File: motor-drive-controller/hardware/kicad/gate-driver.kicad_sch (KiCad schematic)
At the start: 12 parts, among them U3 DRV83053PHP

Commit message: feat(hw09): create links between labels of different hierarchical sheets
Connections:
- net DRV_PWRGD: no longer U3.13 (PWRGD)
- net DRV_nFAULT: no longer U3.8 (~{FAULT})
- net DRV_SCLK renamed DRV.SCLK
- net DRV_SDI renamed DRV.SDI
- net DRV_SDO renamed DRV.SDO
- net DRV_nSCS renamed DRV.nSCS
- net GHA renamed GATE.GHA
- net GHB renamed GATE.GHB
- net GHC renamed GATE.GHC
- net GLA renamed GATE.GLA
- net GLB renamed GATE.GLB
- net GLC renamed GATE.GLC
- net INHA renamed DRV.INHA
- net INHB renamed DRV.INHB
- net INHC renamed DRV.INHC
- net INLA renamed DRV.INLA
- net INLB renamed DRV.INLB
- net INLC renamed DRV.INLC
- net PHASE_A renamed PH.SHA
- net PHASE_B renamed PH.SHB
- net PHASE_C renamed PH.SHC
- net SLA renamed PH.SLA
- net SLB renamed PH.SLB
- net SLC renamed PH.SLC
- net SN_HA renamed CS.SN_LA
- net SN_HB renamed CS.SN_LB
- net SN_HC renamed CS.SN_LC
- net SN_LA renamed CS.SN_HA
- net SN_LB renamed CS.SN_HB
- net SN_LC renamed CS.SN_HC
- new net DRV.PWRGD: U3.13 (PWRGD)
- new net DRV.nFAULT: U3.8 (~{FAULT})
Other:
- moved on the sheet: C16, C17, C20, C21, C24, R12, R15, R16

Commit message: feat(hw09): rename net labels
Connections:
- net DRV_PWRGD is gone; now on net DRV.PWRGD: R16.2
- net DRV_nFAULT is gone; now on net DRV.nFAULT: R15.2
- net CS.SN_HA: now also U3.23 (SN1); no longer U3.24 (SP1)
- net CS.SN_HB: now also U3.21 (SN2); no longer U3.22 (SP2)
- net CS.SN_HC: now also U3.19 (SN3); no longer U3.20 (SP3)
- net CS.SN_LA: now also U3.24 (SP1); no longer U3.23 (SN1)
- net CS.SN_LB: now also U3.22 (SP2); no longer U3.21 (SN2)
- net CS.SN_LC: now also U3.20 (SP3); no longer U3.19 (SN3)
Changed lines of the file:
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@@
+	)
+	(bus_entry
+		(at 95.25 78.74)
+		(size 2.54 2.54)
+		(stroke
+			(width 0)
+			(type default)
+		)
 	)
 	(bus_entry
@@
 	)
 	(bus_entry
+		(at 95.25 96.52)
+		(size 2.54 2.54)
+		(stroke
+			(width 0)
+			(type default)
+		)
+	)
+	(bus_entry
 		(at 95.25 132.08)
 		(size 2.54 2.54)
@@
 	)
 	(bus_entry
+		(at 95.25 81.28)
+		(size 2.54 2.54)
+		(stroke
+			(width 0)
+			(type default)
+		)
+	)
+	(bus_entry
 		(at 158.75 68.58)
 		(size -2.54 -2.54)
@@
 	)
 	(bus_entry
-		(at 95.25 78.74)
-		(size 2.54 2.54)
-		(stroke
-			(width 0)
-			(type default)
-		)
-	)
-	(bus_entry
-		(at 95.25 88.9)
+		(at 95.25 93.98)
 		(size 2.54 2.54)
 		(stroke
@@
 	(bus_entry
 		(at 95.25 66.04)
-		(size 2.54 2.54)
-		(stroke
-			(width 0)
-			(type default)
-		)
-	)
-	(bus_entry
-		(at 95.25 81.28)
 		(size 2.54 2.54)
 		(stroke
@@
 	)
 	(bus_entry
+		(at 95.25 88.9)
+		(size 2.54 2.54)
+		(stroke
+			(width 0)
+			(type default)
+		)
+	)
+	(bus_entry
+		(at 95.25 86.36)
+		(size 2.54 2.54)
+		(stroke
+			(width 0)
+			(type default)
+		)
+	)
+	(bus_entry
 		(at 158.75 63.5)
 		(size -2.54 -2.54)
@@
 	)
 	(bus_entry
-		(at 95.25 93.98)
-		(size 2.54 2.54)
-		(stroke
-			(width 0)
-			(type default)
-		)
-	)
-	(bus_entry
-		(at 95.25 86.36)
-		(size 2.54 2.54)
-		(stroke
-			(width 0)
-			(type default)
-		)
-	)
-	(bus_entry
 		(at 95.25 119.38)
 		(size 2.54 2.54)
@@
 	)
 	(bus_entry
-		(at 95.25 96.52)
-		(size 2.54 2.54)
-		(stroke
-			(width 0)
-			(type default)
-		)
-	)
-	(bus_entry
 		(at 95.25 129.54)
 		(size 2.54 2.54)
@@
 			(width 0)
 			(type default)
+		)
+	)
+	(label "CS.SN_LB"
+		(at 97.79 91.44 0)
+		(effects
+			(font
+				(size 1.27 1.27)
+			)
+			(justify left bottom)
 		)
 	)
@@
 		)
 	)
+	(label "CS.SN_HC"
+		(at 97.79 96.52 0)
+		(effects
+			(font
+				(size 1.27 1.27)
+			)
+			(justify left bottom)
+		)
+	)
 	(label "GATE.GLB"
 		(at 156.21 68.58 180)
@@
 		)
 	)
-	(label "CS.SN_HA"
-		(at 97.79 83.82 0)
-		(effects
-			(font
-				(size 1.27 1.27)
-			)
-			(justify left bottom)
-		)
-	)
-	(label "CS.SN_LA"
-		(at 97.79 81.28 0)
-		(effects
-			(font
-				(size 1.27 1.27)
-			)
-			(justify left bottom)
-		)
-	)
 	(label "PVDD"
 		(at 265.43 40.64 0)
@@
 	)
 	(label "CS.SN_HB"
-		(at 97.79 91.44 0)
+		(at 97.79 88.9 0)
+		(effects
+			(font
+				(size 1.27 1.27)
+			)
+			(justify left bottom)
+		)
+	)
+	(label "CS.SN_LA"
+		(at 97.79 83.82 0)
 		(effects
 			(font
@@
 		)
 	)
-	(label "DRV_nFAULT"
+	(label "DRV.nFAULT"
 		(at 248.92 143.51 180)
 		(effects
@@
 		)
 	)
+	(label "CS.SN_LC"
+		(at 97.79 99.06 0)
+		(effects
+			(font
+				(size 1.27 1.27)
+			)
+			(justify left bottom)
+		)
+	)
 	(label "DRV.SCLK"
 		(at 97.79 129.54 0)
@@
 		)
 	)
-	(label "CS.SN_LB"
-		(at 97.79 88.9 0)
-		(effects
-			(font
-				(size 1.27 1.27)
-			)
-			(justify left bottom)
-		)
-	)
-	(label "CS.SN_HC"
-		(at 97.79 99.06 0)
-		(effects
-			(font
-				(size 1.27 1.27)
-			)
-			(justify left bottom)
-		)
-	)
-	(label "DRV_PWRGD"
+	(label "DRV.PWRGD"
 		(at 256.54 143.51 0)
 		(effects
@@
 		)
 	)
-	(label "CS.SN_LC"
-		(at 97.79 96.52 0)
-		(effects
-			(font
-				(size 1.27 1.27)
-			)
-			(justify left bottom)
-		)
-	)
 	(label "DRV.INHB"
 		(at 97.79 111.76 0)
 		(effects
 			(font
+				(size 1.27 1.27)
+			)
+			(justify left bottom)
+		)
+	)
+	(label "CS.SN_HA"
+		(at 97.79 81.28 0)
+		(effects
+			(font

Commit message: feat(hw09): add ISENSE ADC channels and update schematics
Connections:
- net ISENSE.SO1: now reaches U3.16 (SO1)
- net ISENSE.SO2: now reaches U3.17 (SO2)
- net ISENSE.SO3: now reaches U3.18 (SO3)
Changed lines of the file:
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@@
+	)
+	(bus_entry
+		(at 158.75 88.9)
+		(size -2.54 -2.54)
+		(stroke
+			(width 0)
+			(type default)
+		)
 	)
 	(bus_entry
@@
 		(at 95.25 96.52)
 		(size 2.54 2.54)
+		(stroke
+			(width 0)
+			(type default)
+		)
+	)
+	(bus_entry
+		(at 158.75 86.36)
+		(size -2.54 -2.54)
 		(stroke
 			(width 0)
@@
 	)
 	(bus_entry
+		(at 158.75 83.82)
+		(size -2.54 -2.54)
+		(stroke
+			(width 0)
+			(type default)
+		)
+	)
+	(bus_entry
 		(at 95.25 129.54)
 		(size 2.54 2.54)
@@
 	(wire
 		(pts
+			(xy 143.51 86.36) (xy 156.21 86.36)
+		)
+		(stroke
+			(width 0)
+			(type default)
+		)
+	)
+	(wire
+		(pts
 			(xy 96.52 147.32) (xy 92.71 147.32)
 		)
@@
 	(wire
 		(pts
+			(xy 143.51 81.28) (xy 156.21 81.28)
+		)
+		(stroke
+			(width 0)
+			(type default)
+		)
+	)
+	(wire
+		(pts
 			(xy 248.92 143.51) (xy 248.92 138.43)
 		)
@@
 	(bus
 		(pts
+			(xy 165.1 91.44) (xy 158.75 91.44)
+		)
+		(stroke
+			(width 0)
+			(type default)
+		)
+	)
+	(bus
+		(pts
 			(xy 95.25 73.66) (xy 95.25 53.34)
 		)
@@
 		)
 	)
+	(wire
+		(pts
+			(xy 143.51 83.82) (xy 156.21 83.82)
+		)
+		(stroke
+			(width 0)
+			(type default)
+		)
+	)
 	(bus
 		(pts
@@
 		(pts
 			(xy 97.79 129.54) (xy 107.95 129.54)
+		)
+		(stroke
+			(width 0)
+			(type default)
+		)
+	)
+	(bus
+		(pts
+			(xy 158.75 83.82) (xy 158.75 91.44)
 		)
 		(stroke
@@
 		)
 	)
+	(label "ISENSE.SO2"
+		(at 156.21 83.82 180)
+		(effects
+			(font
+				(size 1.27 1.27)
+			)
+			(justify right bottom)
+		)
+	)
 	(label "DRV.PWRGD"
 		(at 256.54 143.51 0)
@@
 		)
 	)
+	(label "ISENSE.SO3"
+		(at 156.21 86.36 180)
+		(effects
+			(font
+				(size 1.27 1.27)
+			)
+			(justify right bottom)
+		)
+	)
 	(label "AVDD"
 		(at 247.65 86.36 0)
@@
 			)
 			(justify bottom)
+		)
+	)
+	(label "ISENSE.SO1"
+		(at 156.21 81.28 180)
+		(effects
+			(font
+				(size 1.27 1.27)
+			)
+			(justify right bottom)
 		)
 	)
@@
 		(effects
 			(font
+				(size 1.27 1.27)
+			)
+			(justify left)
+		)
+	)
+	(hierarchical_label "ISENSE{ADC3}"
+		(shape output)
+		(at 165.1 91.44 0)
+		(effects
+			(font

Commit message: feat(hw09): update ADC channel names and schematic references to ANALOG prefix
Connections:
- net ISENSE.SO1 renamed ANALOG.SO1
- net ISENSE.SO2 renamed ANALOG.SO2
- net ISENSE.SO3 renamed ANALOG.SO3
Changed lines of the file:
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@@
 		)
 	)
-	(label "ISENSE.SO2"
+	(label "ANALOG.SO2"
 		(at 156.21 83.82 180)
 		(effects
@@
 		)
 	)
-	(label "ISENSE.SO3"
+	(label "ANALOG.SO3"
 		(at 156.21 86.36 180)
 		(effects
@@
 		)
 	)
-	(label "ISENSE.SO1"
+	(label "ANALOG.SO1"
 		(at 156.21 81.28 180)
 		(effects
@@
 		)
 	)
-	(hierarchical_label "ISENSE{ADC3}"
+	(hierarchical_label "ANALOG{AIN4}"
 		(shape output)
 		(at 165.1 91.44 0)

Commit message: fix(hw09): fix ERC issues
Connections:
- net DRV.EN_GATE: now reaches U3.1 (EN_GATE)
- net DRV.WAKE: now reaches U3.47 (WAKE)
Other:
- moved on the sheet: C16, C17, C18, C19, C20, C23, C24, R12, R15, R16

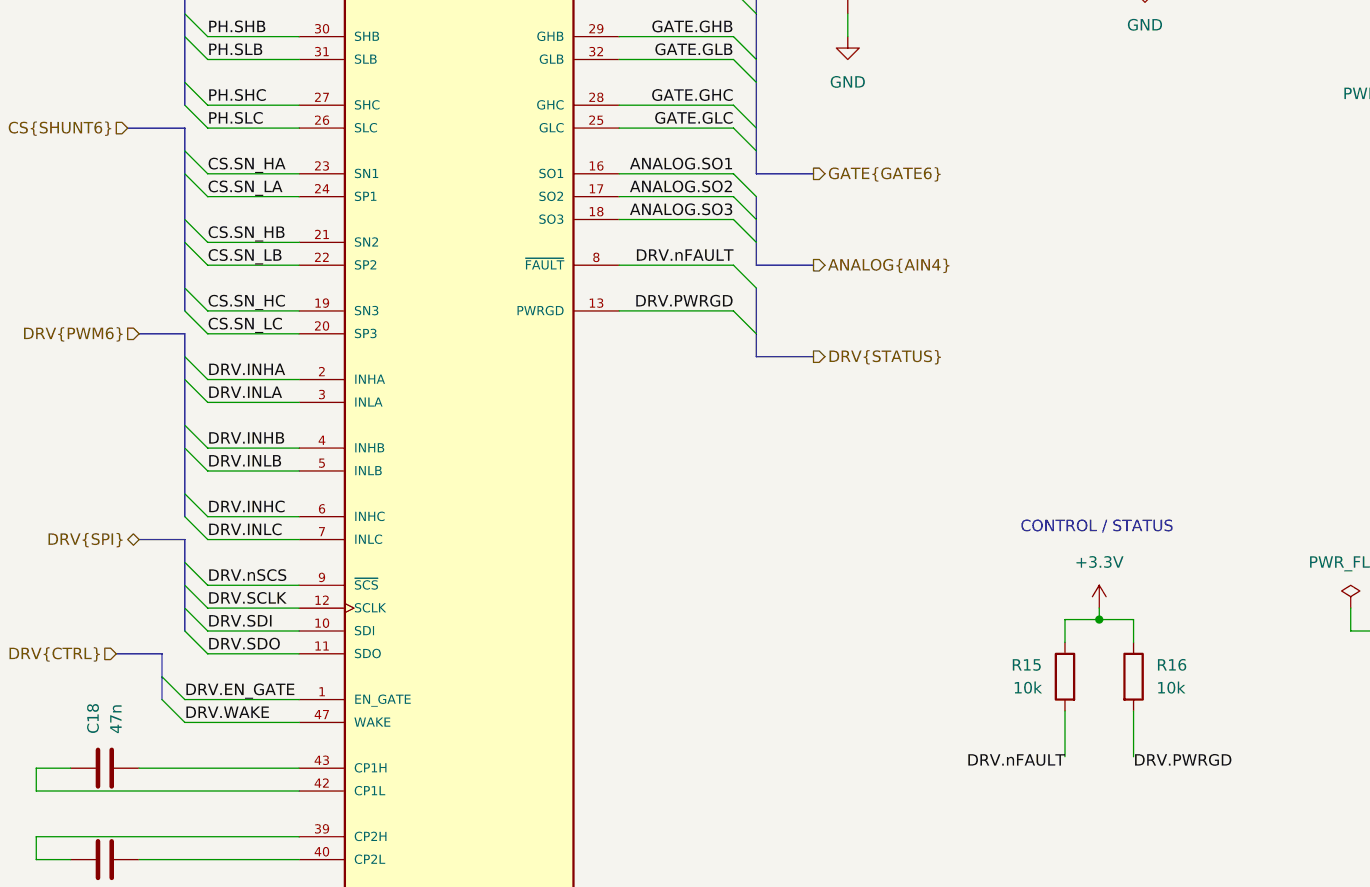
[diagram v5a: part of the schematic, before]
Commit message: feat(hw09): add EN_GATE control and WAKE signal handling in hardware design
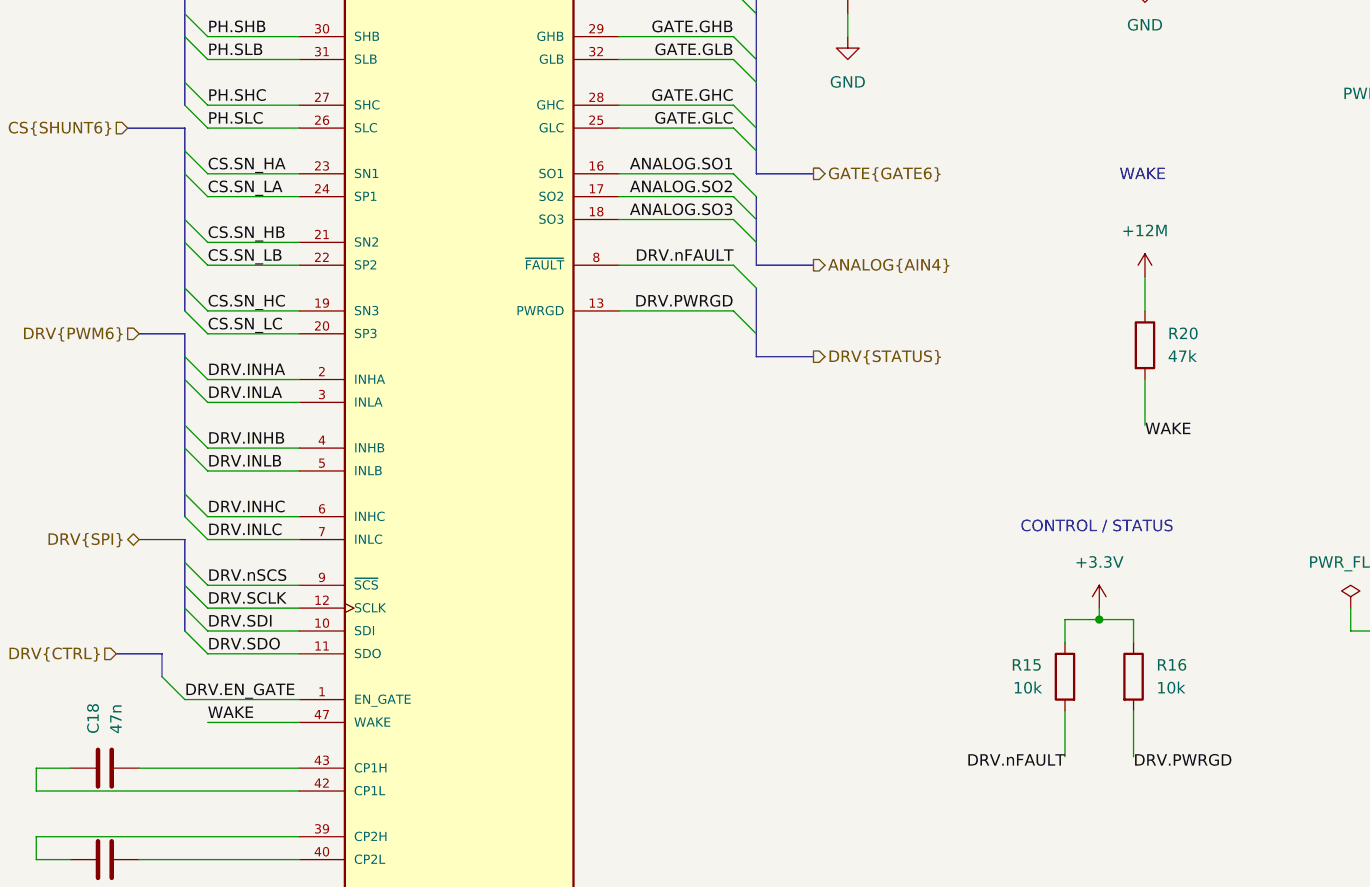
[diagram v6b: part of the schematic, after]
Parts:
- added R20: 47k, symbol Device:R
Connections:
- net +12M: now also R20.1
- net DRV.WAKE renamed WAKE
- net WAKE: now also R20.2
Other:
- note added: "WAKE"
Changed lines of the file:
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@@
 		(title "Gate Driver — DRV8305")
 	)
+	(text "WAKE"
+		(exclude_from_sim no)
+		(at 201.676 81.534 0)
+		(effects
+			(font
+				(size 1.27 1.27)
+			)
+		)
+	)
 	(text "Живлення"
 		(exclude_from_sim no)
@@
 	)
 	(bus_entry
+		(at 92.71 137.16)
+		(size 2.54 2.54)
+		(stroke
+			(width 0)
+			(type default)
+		)
+	)
+	(bus_entry
 		(at 95.25 93.98)
 		(size 2.54 2.54)
@@
 	)
 	(bus_entry
-		(at 92.71 139.7)
-		(size 2.54 2.54)
-		(stroke
-			(width 0)
-			(type default)
-		)
-	)
-	(bus_entry
-		(at 92.71 137.16)
-		(size 2.54 2.54)
-		(stroke
-			(width 0)
-			(type default)
-		)
-	)
-	(bus_entry
 		(at 95.25 129.54)
 		(size 2.54 2.54)
@@
 	(wire
 		(pts
-			(xy 143.51 86.36) (xy 156.21 86.36)
+			(xy 201.93 104.14) (xy 201.93 109.22)
 		)
 		(stroke
@@
 	(wire
 		(pts
-			(xy 224.79 132.08) (xy 237.49 132.08)
+			(xy 143.51 86.36) (xy 156.21 86.36)
 		)
 		(stroke
@@
 	(wire
 		(pts
-			(xy 240.03 62.23) (xy 240.03 68.58)
+			(xy 224.79 132.08) (xy 237.49 132.08)
 		)
 		(stroke
@@
 	(wire
 		(pts
-			(xy 82.55 147.32) (xy 78.74 147.32)
+			(xy 240.03 62.23) (xy 240.03 68.58)
 		)
 		(stroke
@@
 	(wire
 		(pts
-			(xy 95.25 142.24) (xy 107.95 142.24)
+			(xy 82.55 147.32) (xy 78.74 147.32)
 		)
 		(stroke
@@
 		)
 	)
+	(wire
+		(pts
+			(xy 95.25 139.7) (xy 107.95 139.7)
+		)
+		(stroke
+			(width 0)
+			(type default)
+		)
+	)
 	(bus
 		(pts
@@
 	(bus
 		(pts
-			(xy 92.71 139.7) (xy 92.71 134.62)
+			(xy 92.71 137.16) (xy 92.71 134.62)
 		)
 		(stroke
@@
 	(wire
 		(pts
-			(xy 240.03 41.91) (xy 240.03 48.26)
+			(xy 201.93 92.71) (xy 201.93 96.52)
 		)
 		(stroke
@@
 		)
 	)
-	(bus
+	(wire
 		(pts
-			(xy 87.63 134.62) (xy 92.71 134.62)
+			(xy 240.03 41.91) (xy 240.03 48.26)
 		)
 		(stroke
@@
 	(bus
 		(pts
-			(xy 90.17 121.92) (xy 95.25 121.92)
+			(xy 87.63 134.62) (xy 92.71 134.62)
 		)
 		(stroke
@@
 		)
 	)
-	(wire
+	(bus
 		(pts
-			(xy 95.25 139.7) (xy 107.95 139.7)
+			(xy 90.17 121.92) (xy 95.25 121.92)
 		)
 		(stroke
@@
 		)
 	)
+	(wire
+		(pts
+			(xy 97.79 142.24) (xy 107.95 142.24)
+		)
+		(stroke
+			(width 0)
+			(type default)
+		)
+	)
 	(bus
 		(pts
@@
 		)
 	)
-	(label "DRV.EN_GATE"
-		(at 95.25 139.7 0)
+	(label "PVDD"
+		(at 156.21 45.72 180)
 		(effects
 			(font
 				(size 1.27 1.27)
 			)
-			(justify left bottom)
+			(justify right bottom)
 		)
 	)
-	(label "PVDD"
-		(at 156.21 45.72 180)
+	(label "AVDD"
+		(at 156.21 40.64 180)
 		(effects
 			(font
@@
 		)
 	)
-	(label "AVDD"
-		(at 156.21 40.64 180)
+	(label "DRV.EN_GATE"
+		(at 95.25 139.7 0)
 		(effects
 			(font
 				(size 1.27 1.27)
 			)
-			(justify right bottom)
+			(justify left bottom)
 		)
 	)
@@
 		)
 	)
+	(label "WAKE"
+		(at 97.79 142.24 0)
+		(effects
+			(font
+				(size 1.27 1.27)
+			)
+			(justify left bottom)
+		)
+	)
 	(label "PH.SLC"
 		(at 97.79 76.2 0)
@@
 		)
 	)
+	(label "WAKE"
+		(at 201.93 109.22 0)
+		(effects
+			(font
+				(size 1.27 1.27)
+			)
+			(justify top)
+		)
+	)
 	(label "DRV.INLB"
 		(at 97.79 114.3 0)
@@
 		)
 	)
-	(label "DRV.WAKE"
-		(at 95.25 142.24 0)
-		(effects
-			(font
-				(size 1.27 1.27)
-			)
-			(justify left bottom)
-		)
-	)
 	(label "PH.SLB"
 		(at 97.79 68.58 0)
@@
 	)
 	(symbol
+		(lib_id "Device:R")
+		(at 201.93 100.33 0)
+		(unit 1)
+		(body_style 1)
+		(exclude_from_sim no)
+		(in_bom yes)
+		(on_board yes)
+		(in_pos_files yes)
+		(dnp no)
+		(fields_autoplaced yes)
+		(property "Reference" "R20"
+			(at 204.47 99.0599 0)
+			(show_name no)
+			(do_not_autoplace no)
+			(effects
+				(font
+					(size 1.27 1.27)
+				)
+				(justify left)
+			)
+		)
+		(property "Value" "47k"
+			(at 204.47 101.5999 0)
+			(show_name no)
+			(do_not_autoplace no)
+			(effects
+				(font
+					(size 1.27 1.27)
+				)
+				(justify left)
+			)
+		)
+		(property "Footprint" ""
+			(at 200.152 100.33 90)
+			(hide yes)
+			(show_name no)
+			(do_not_autoplace no)
+			(effects
+				(font
+					(size 1.27 1.27)
+				)
+			)
+		)
+		(property "Datasheet" ""
+			(at 201.93 100.33 0)
+			(hide yes)
+			(show_name no)
+			(do_not_autoplace no)
+			(effects
+				(font
+					(size 1.27 1.27)
+				)
+			)
+		)
+		(property "Description" "Resistor"
+			(at 201.93 100.33 0)
+			(hide yes)
+			(show_name no)
+			(do_not_autoplace no)
+			(effects
+				(font
+					(size 1.27 1.27)
+				)
+			)
+		)
+		(pin "1"
+		)
+		(pin "2"
+		)
+		(instances
+			(project "motor-drive-controller"
+				(path "/b8e0307a-d356-4cd3-91c6-dd251b6e910b/0c161995-df7f-44eb-a617-0aa9a9de53ee"
+					(reference "R20")
+					(unit 1)
+				)
+			)
+		)
+	)
+	(symbol
 		(lib_id "power:+3.3V")
 		(at 201.93 43.18 0)
@@
 					(unit 1)
 				)
+			)
+		)
+	)
+	(symbol
+		(lib_id "power:+12V")
+		(at 201.93 92.71 0)
+		(unit 1)
+		(body_style 1)
+		(exclude_from_sim no)
+		(in_bom yes)
+		(on_board yes)
+		(in_pos_files yes)
+		(dnp no)
+		(fields_autoplaced yes)
+		(property "Reference" "#PWR052"
+			(at 201.93 96.52 0)
+			(hide yes)
+			(show_name no)
+			(do_not_autoplace no)
+			(effects
+				(font
+					(size 1.27 1.27)
+				)
+			)
+		)
+		(property "Value" "+12M"
+			(at 201.93 87.63 0)
+			(show_name no)
+			(do_not_autoplace no)
+			(effects
+				(font
+					(size 1.27 1.27)
+				)
+			)
+		)
+		(property "Footprint" ""
+			(at 201.93 92.71 0)
+			(hide yes)
+			(show_name no)
+			(do_not_autoplace no)
+			(effects
+				(font
+					(size 1.27 1.27)
+				)
+			)
+		)
+		(property "Datasheet" ""
+			(at 201.93 92.71 0)
+			(hide yes)
+			(show_name no)
+			(do_not_autoplace no)
+			(effects
+				(font
+					(size 1.27 1.27)
+				)
+			)
+		)
+		(property "Description" "Power symbol creates a global label with name \"+12V\""
+			(at 201.93 92.71 0)
+			(hide yes)
+			(show_name no)
+			(do_not_autoplace no)
+			(effects
+				(font
+					(size 1.27 1.27)
+				)
+			)
+		)
+		(pin "1"
+		)
+		(instances
+			(project "motor-drive-controller"
+				(path "/b8e0307a-d356-4cd3-91c6-dd251b6e910b/0c161995-df7f-44eb-a617-0aa9a9de53ee"
+					(reference "#PWR052")
+					(unit 1)
+				)

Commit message: fix(hw09): fix ERC issues
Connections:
- net GND is gone; now on net EP: C16.2, C17.2, C20.2, C23.2, C24.2, U3.14 (GND), U3.45 (GND)
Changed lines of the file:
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@@
 	)
 	(junction
+		(at 148.59 165.1)
+		(diameter 0)
+		(color 0 0 0 0)
+	)
+	(junction
 		(at 237.49 132.08)
 		(diameter 0)
@@
 	(wire
 		(pts
+			(xy 191.77 43.18) (xy 191.77 45.72)
+		)
+		(stroke
+			(width 0)
+			(type default)
+		)
+	)
+	(wire
+		(pts
 			(xy 97.79 134.62) (xy 107.95 134.62)
 		)
@@
 	(wire
 		(pts
+			(xy 191.77 45.72) (xy 201.93 45.72)
+		)
+		(stroke
+			(width 0)
+			(type default)
+		)
+	)
+	(wire
+		(pts
 			(xy 143.51 162.56) (xy 148.59 162.56)
 		)
@@
 	(wire
 		(pts
+			(xy 148.59 167.64) (xy 148.59 165.1)
+		)
+		(stroke
+			(width 0)
+			(type default)
+		)
+	)
+	(wire
+		(pts
 			(xy 259.08 129.54) (xy 259.08 132.08)
 		)
@@
 	(wire
 		(pts
+			(xy 143.51 165.1) (xy 148.59 165.1)
+		)
+		(stroke
+			(width 0)
+			(type default)
+		)
+	)
+	(wire
+		(pts
 			(xy 255.27 41.91) (xy 255.27 45.72)
 		)
@@
 	)
 	(symbol
+		(lib_id "power:PWR_FLAG")
+		(at 191.77 43.18 0)
+		(unit 1)
+		(body_style 1)
+		(exclude_from_sim no)
+		(in_bom yes)
+		(on_board yes)
+		(in_pos_files yes)
+		(dnp no)
+		(fields_autoplaced yes)
+		(property "Reference" "#FLG013"
+			(at 191.77 41.275 0)
+			(hide yes)
+			(show_name no)
+			(do_not_autoplace no)
+			(effects
+				(font
+					(size 1.27 1.27)
+				)
+			)
+		)
+		(property "Value" "PWR_FLAG"
+			(at 191.77 38.1 0)
+			(show_name no)
+			(do_not_autoplace no)
+			(effects
+				(font
+					(size 1.27 1.27)
+				)
+			)
+		)
+		(property "Footprint" ""
+			(at 191.77 43.18 0)
+			(hide yes)
+			(show_name no)
+			(do_not_autoplace no)
+			(effects
+				(font
+					(size 1.27 1.27)
+				)
+			)
+		)
+		(property "Datasheet" ""
+			(at 191.77 43.18 0)
+			(hide yes)
+			(show_name no)
+			(do_not_autoplace no)
+			(effects
+				(font
+					(size 1.27 1.27)
+				)
+			)
+		)
+		(property "Description" "Special symbol for telling ERC where power comes from"
+			(at 191.77 43.18 0)
+			(hide yes)
+			(show_name no)
+			(do_not_autoplace no)
+			(effects
+				(font
+					(size 1.27 1.27)
+				)
+			)
+		)
+		(pin "1"
+		)
+		(instances
+			(project "motor-drive-controller"
+				(path "/b8e0307a-d356-4cd3-91c6-dd251b6e910b/0c161995-df7f-44eb-a617-0aa9a9de53ee"
+					(reference "#FLG013")
+					(unit 1)
+				)
+			)
+		)
+	)
+	(symbol
 		(lib_id "power:GND")
 		(at 237.49 148.59 0)
@@
 	(symbol
 		(lib_id "power:GND")
-		(at 148.59 165.1 0)
+		(at 148.59 167.64 0)
 		(unit 1)
 		(body_style 1)
@@
 		(fields_autoplaced yes)
 		(property "Reference" "#PWR033"
-			(at 148.59 171.45 0)
+			(at 148.59 173.99 0)
 			(hide yes)
 			(show_name no)
@@
 		)
 		(property "Value" "GND"
-			(at 148.59 170.18 0)
+			(at 148.59 172.72 0)
 			(show_name no)
 			(do_not_autoplace no)
@@
 		)
 		(property "Footprint" ""
-			(at 148.59 165.1 0)
+			(at 148.59 167.64 0)
 			(hide yes)
 			(show_name no)
@@
 		)
 		(property "Datasheet" ""
-			(at 148.59 165.1 0)
+			(at 148.59 167.64 0)
 			(hide yes)
 			(show_name no)
@@
 		)
 		(property "Description" "Power symbol creates a global label with name \"GND\" , ground"
-			(at 148.59 165.1 0)
+			(at 148.59 167.64 0)
 			(hide yes)
 			(show_name no)
